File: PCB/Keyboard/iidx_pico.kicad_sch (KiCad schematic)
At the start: 77 parts, among them J1 CONN_01x05, J2 CONN_01x05, J3 PJ393-8P, SW1 SWITCH_SPST, SW10 SWITCH_SPST, SW11 SWITCH_SPST, SW12 Tact_4pin, SW13 Tact_4pin, SW2 SWITCH_SPST, SW3 SWITCH_SPST, SW4 SWITCH_SPST, SW5 SWITCH_SPST, SW6 SWITCH_SPST, SW7 SWITCH_SPST, SW8 SWITCH_SPST, SW9 SWITCH_SPST, U1 Pico, U2 SN74LV1T34DBV, U3 SN74LV1T34DBV

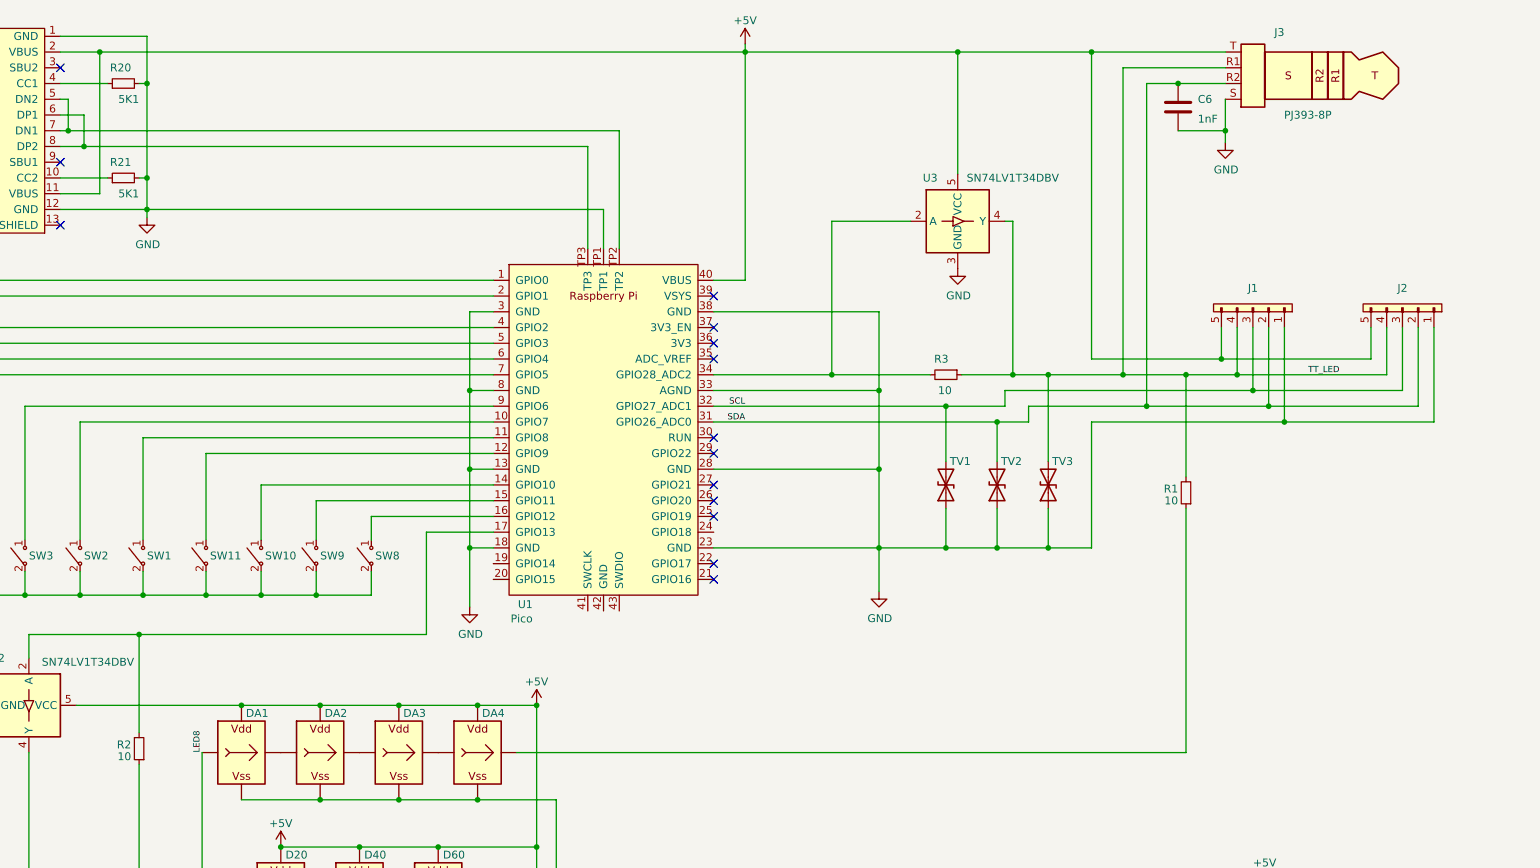
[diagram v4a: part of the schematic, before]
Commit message: Removal of confusion parts in PCB
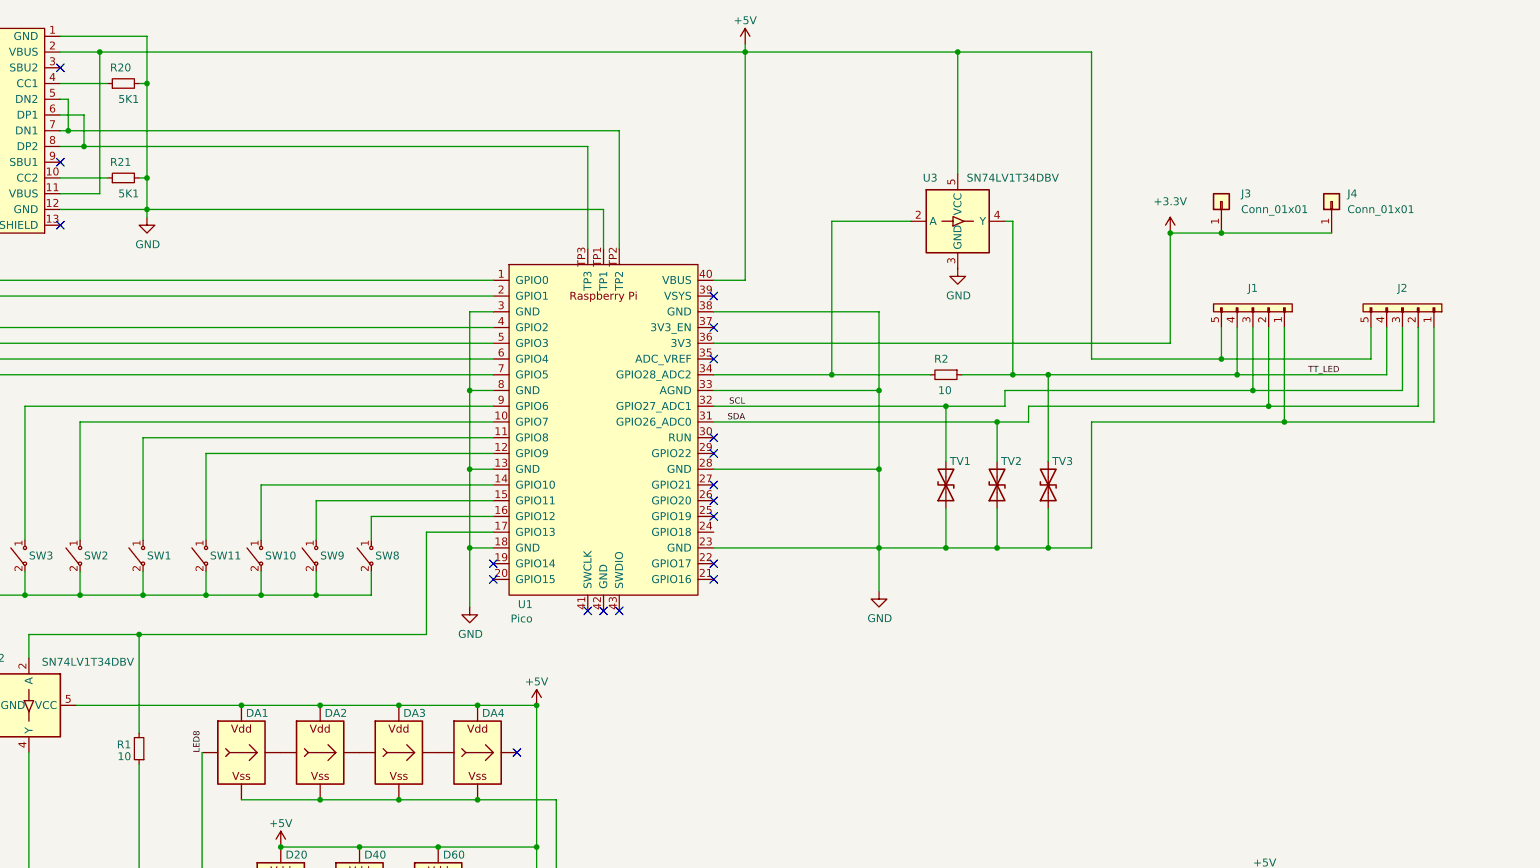
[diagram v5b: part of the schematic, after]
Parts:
- removed C6: 1nF, Capacitor_SMD:C_0805_2012Metric, symbol Device:C
- removed J3: PJ393-8P, iidx_pico:PJ393-8P, symbol Connector:AudioPlug4
- removed R1: 10, Resistor_SMD:R_0603_1608Metric, symbol Device:R_Small
- added J3, J4: Conn_01x01, iidx_pico:Solder_1P, symbol Connector_Generic:Conn_01x01
- renumbered R2 to R1, R3 to R2
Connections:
- net +3.3V: now reaches U1.36 (3V3)
- net +3.3V: now also J3.1 (Pin_1), J4.1 (Pin_1)
- no-connect marks 14 -> 19

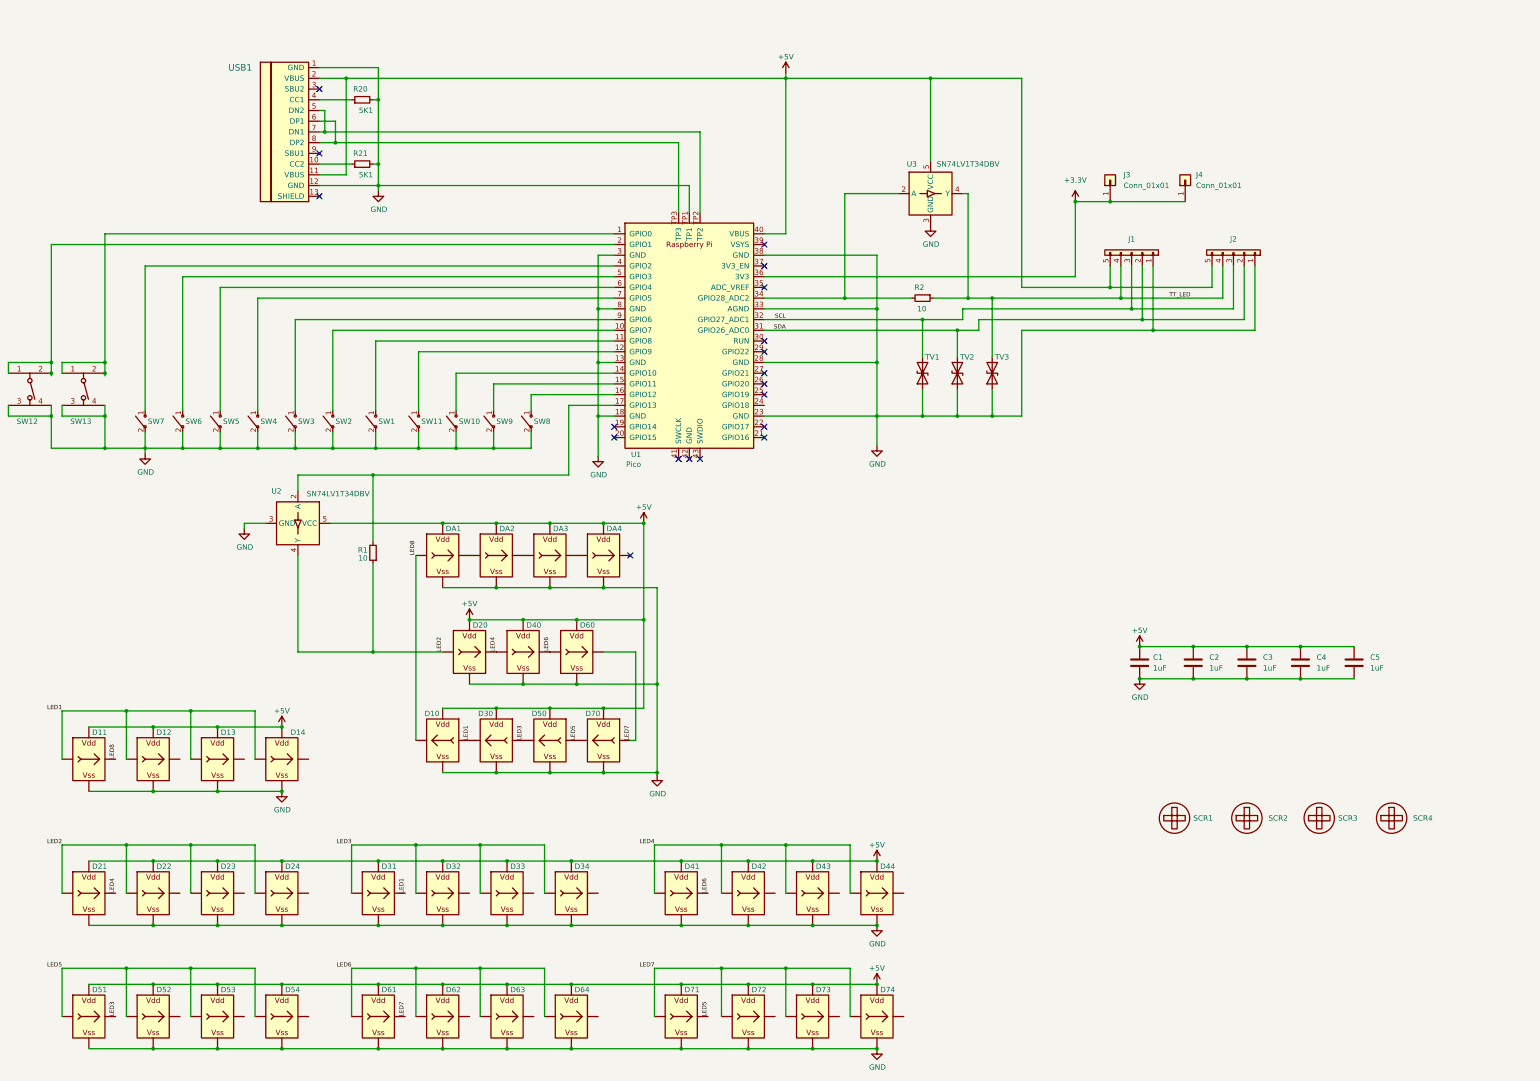
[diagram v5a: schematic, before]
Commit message: PCB v1.4 (sensor on board)
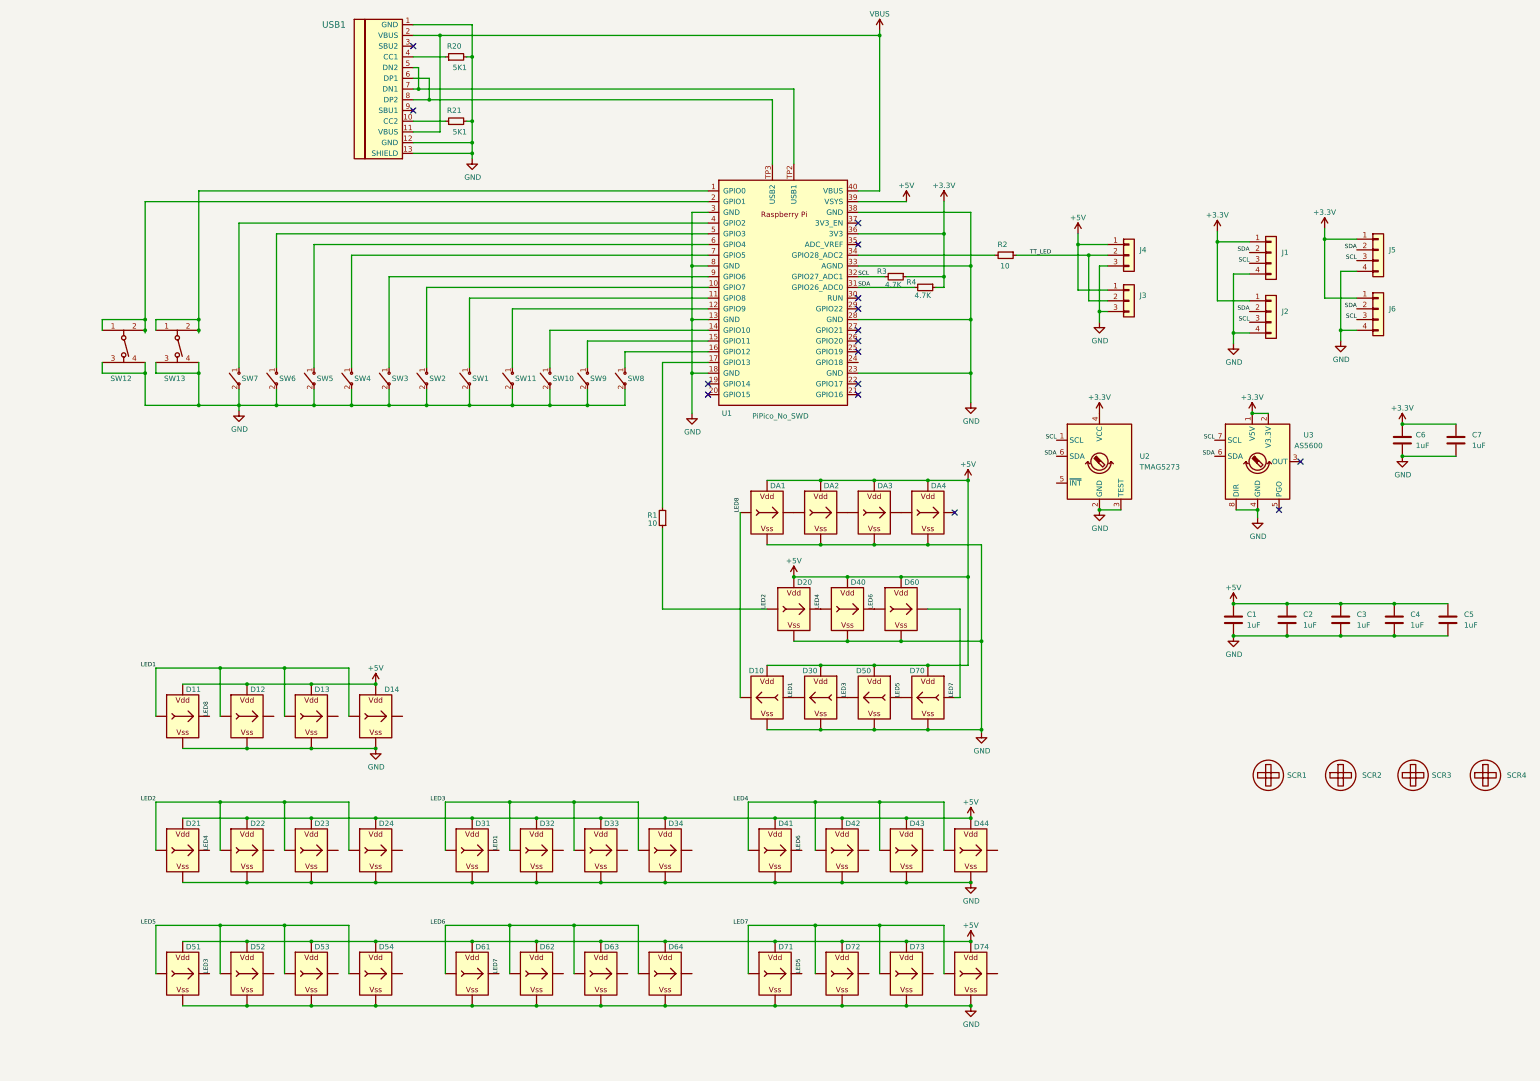
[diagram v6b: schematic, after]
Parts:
- removed J1, J2: CONN_01x05, iidx_pico:Pogo_5P_Female, symbol agg:CONN_01x05
- removed J3, J4: Conn_01x01, iidx_pico:Solder_1P, symbol Connector_Generic:Conn_01x01
- removed TV1, TV2, TV3: D_TVS, Diode_SMD:D_SOD-323_HandSoldering, symbol Device:D_TVS
- removed U1: Pico, MCU_RaspberryPi_and_Boards:RPi_Pico_SMD, symbol MCU_RaspberryPi_and_Boards:Pico
- removed U2, U3: SN74LV1T34DBV, iidx_pico:SOT-23-5_Jumper, symbol Logic_LevelTranslator:SN74LV1T34DBV
- added C6, C7: 1uF, Capacitor_SMD:C_0603_1608Metric_Pad1.08x0.95mm_HandSolder, symbol Device:C
- added J1, J2: Spin, iidx_pico:SH1.0_4P_Solder_Combo, symbol Connector_Generic:Conn_01x04
- added J3, J4: RGB, iidx_pico:SH1.0_3P_Solder_Combo, symbol Connector_Generic:Conn_01x03
- added J5, J6: Spin, iidx_pico:P2.0_4P_Solder, symbol Connector_Generic:Conn_01x04
- added R3, R4: 4.7K, Resistor_SMD:R_0603_1608Metric_Pad0.98x0.95mm_HandSolder, symbol Device:R_Small
- added U1: PiPico_No_SWD, iidx_pico:RPi_Pico_SMD_Pins_No_SWD, symbol iidx_pico:PiPico_No_SWD
- added U2: TMAG5273, Package_TO_SOT_SMD:TSOT-23-6_HandSoldering, symbol iidx_pico:TMAG5273
- added U3: AS5600, Package_SO:SOIC-8_3.9x4.9mm_P1.27mm, symbol iidx_pico:AS5600
- C1, C2, C3, C4, C5: footprint Capacitor_SMD:C_0805_2012Metric -> Capacitor_SMD:C_0603_1608Metric_Pad1.08x0.95mm_HandSolder
- R1, R2, R20, R21: footprint Resistor_SMD:R_0603_1608Metric -> Resistor_SMD:R_0603_1608Metric_Pad0.98x0.95mm_HandSolder
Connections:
- net +3.3V: now also C6.1, C7.1, J1.1 (Pin_1), J2.1 (Pin_1), J5.1 (Pin_1), J6.1 (Pin_1), R3.1, R4.1, U1.36 (3V3), U2.4 (VCC), U3.1 (V5V), U3.2 (V3.3V)
- net +5V: now also J3.1 (Pin_1), J4.1 (Pin_1), U1.39 (VSYS); no longer USB1.11 (VBUS), USB1.2 (VBUS)
- net GND: now also USB1.13 (SHIELD), C6.2, C7.2, J1.4 (Pin_4), J2.4 (Pin_4), J3.3 (Pin_3), J4.3 (Pin_3), J5.4 (Pin_4), J6.4 (Pin_4), U1.13 (GND), U1.18 (GND), U1.23 (GND), U1.28 (GND), U1.3 (GND), U1.33 (AGND), U1.38 (GND), U1.8 (GND), U2.2 (GND), U2.3 (TEST), U3.4 (GND), U3.8 (DIR)
- net SCL: now also J1.3 (Pin_3), J2.3 (Pin_3), J5.3 (Pin_3), J6.3 (Pin_3), R3.2, U1.32 (GPIO27_ADC1), U2.1 (SCL), U3.7 (SCL)
- net SDA: now also J1.2 (Pin_2), J2.2 (Pin_2), J5.2 (Pin_2), J6.2 (Pin_2), R4.2, U1.31 (GPIO26_ADC0), U2.6 (SDA), U3.6 (SDA)
- net TT_LED: now also J3.2 (Pin_2), J4.2 (Pin_2)
- net at SW13.1, SW13.2: now also U1.1 (GPIO0)
- net at SW2.1 ("~{"}): now also U1.10 (GPIO7)
- net at SW1.1 ("~{"}): now also U1.11 (GPIO8)
- net at SW11.1 ("~{"}): now also U1.12 (GPIO9)
- net at SW10.1 ("~{"}): now also U1.14 (GPIO10)
- net at SW9.1 ("~{"}): now also U1.15 (GPIO11)
- net at SW8.1 ("~{"}): now also U1.16 (GPIO12)
- net at R1.2: now also U1.17 (GPIO13)
- net at SW12.1, SW12.2: now also U1.2 (GPIO1)
- net at R2.2: now also U1.34 (GPIO28_ADC2)
- net at SW7.1 ("~{"}): now also U1.4 (GPIO2)
- net at SW6.1 ("~{"}): now also U1.5 (GPIO3)
- net at SW5.1 ("~{"}): now also U1.6 (GPIO4)
- net at SW4.1 ("~{"}): now also U1.7 (GPIO5)
- net at SW3.1 ("~{"}): now also U1.9 (GPIO6)
- net at USB1.5 (DN2), USB1.7 (DN1): now also U1.TP2 (USB1)
- net at USB1.6 (DP1), USB1.8 (DP2): now also U1.TP3 (USB2)
- new net VBUS: U1.40 (VBUS), USB1.11 (VBUS), USB1.2 (VBUS)
- no-connect marks 19 -> 16
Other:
- moved on the sheet: C1, C2, C3, C4, C5, D10, D11, D12, D13, D14, D20, D21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
